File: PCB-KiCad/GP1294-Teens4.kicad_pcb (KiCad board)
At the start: 2 copper layers, 178.5 x 99.9 mm, 37 parts, among them IC1 74132D, IC2 XL6009, IC3 ZXBM5210, SW1 SW_Push, SW2 SW_Push, SW3 SW_Push, SW4 SW_Push, SW5 SW_Push, U3 R-78B5.0-2.0

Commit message: GP12.. better case and stuff
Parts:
- added R10: 100, Resistor_SMD:R_0603_1608Metric, F.Cu at (154.9, 110.2)
- added R11: 10k, Resistor_SMD:R_0603_1608Metric, F.Cu at (185.9, 74.2)
- added R12: 10k, Resistor_SMD:R_0603_1608Metric, F.Cu at (185.9, 76.7)
- added U5: ATtiny84A-P, Package_DIP:DIP-14_W7.62mm, B.Cu at (159.0, 113.3)
- added U6: 74HC165, Package_SO:SO-16_3.9x9.9mm_P1.27mm, F.Cu at (160.0, 140.0)
- added U7: 74HC165, Package_SO:SO-16_3.9x9.9mm_P1.27mm, F.Cu at (121.4, 109.5)
- SW1, SW2, SW3, SW4, SW5: value SW_Push -> SW_DPDT_x2; footprint Button_Switch_THT:SW_PUSH-12mm_Wuerth-430476085716 -> VFDs-Library:SwitchMS500Ecut
- moved SW5 82.5 mm to (111.7, 125.1)
- moved SW1 69.6 mm to (188.2, 125.0)
- moved SW4 45.2 mm to (130.8, 125.0)
- moved SW2 32.7 mm to (169.2, 125.0)
- moved R8 20.2 mm to (176.1, 69.1), turned to 180 degrees
- moved R6 20.0 mm to (167.1, 69.1), turned to 0 degrees
- moved R7 17.8 mm to (167.1, 71.6), turned to 0 degrees
- moved R9 17.5 mm to (176.0, 71.6), turned to 180 degrees
- moved R4 13.5 mm to (215.5, 74.2)
- moved IC3 11.7 mm to (215.4, 68.3)
- moved SW3 11.0 mm to (150.0, 125.0)
- moved C4 10.7 mm to (207.0, 83.6)
- moved R1 10.1 mm to (191.6, 69.3)
- moved C1 10.0 mm to (191.6, 66.3)
- moved IC1 9.40 mm to (201.7, 70.4)
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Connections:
- ENC1 pad A: unconnected-(ENC1-PadA) -> /inputs/enc1a
- ENC1 pad B: unconnected-(ENC1-PadB) -> /inputs/enc1b
- ENC1 pad C: unconnected-(ENC1-PadC) -> GND
- ENC1 pad S1: unconnected-(ENC1-PadS1) -> /inputs/enc1c
- ENC1 pad S2: unconnected-(ENC1-PadS2) -> GND
- ENC2 pad A: unconnected-(ENC2-PadA) -> /inputs/enc2a
- ENC2 pad B: unconnected-(ENC2-PadB) -> /inputs/enc2b
- ENC2 pad C: unconnected-(ENC2-PadC) -> GND
- ENC2 pad S1: unconnected-(ENC2-PadS1) -> /inputs/enc2c
- ENC2 pad S2: unconnected-(ENC2-PadS2) -> GND
- SW1 pad 1: GND -> Net-(SW1A-A)
- SW1 pad 2: Net-(U2-5) -> GND
- SW2 pad 1: unconnected-(SW2-Pad1) -> Net-(SW2A-A)
- SW2 pad 2: unconnected-(SW2-Pad2) -> GND
- SW3 pad 1: GND -> Net-(SW3A-A)
- SW3 pad 2: Net-(U2-3) -> GND
- SW4 pad 1: GND -> Net-(SW4A-A)
- SW4 pad 2: Net-(U2-4) -> GND
- SW5 pad 1: unconnected-(SW5-Pad1) -> Net-(SW5A-A)
- SW5 pad 2: unconnected-(SW5-Pad2) -> GND
- U2 pad 18: unconnected-(U2-A2-Pad18) -> /SDA
- U2 pad 19: unconnected-(U2-A3-Pad19) -> /SCL
- U2 pad 5: Net-(U2-3) -> unconnected-(U2-3-Pad5)
- U2 pad 6: Net-(U2-4) -> unconnected-(U2-4-Pad6)
- U2 pad 7: Net-(U2-5) -> unconnected-(U2-5-Pad7)
- U4 pad 11: unconnected-(U4-SDA-Pad11) -> /SDA
- U4 pad 13: unconnected-(U4-SCL-Pad13) -> /SCL
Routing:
- net GND: vias 3 -> 5
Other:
- board size 178.5 x 99.9 mm -> 178.3 x 100.1 mm

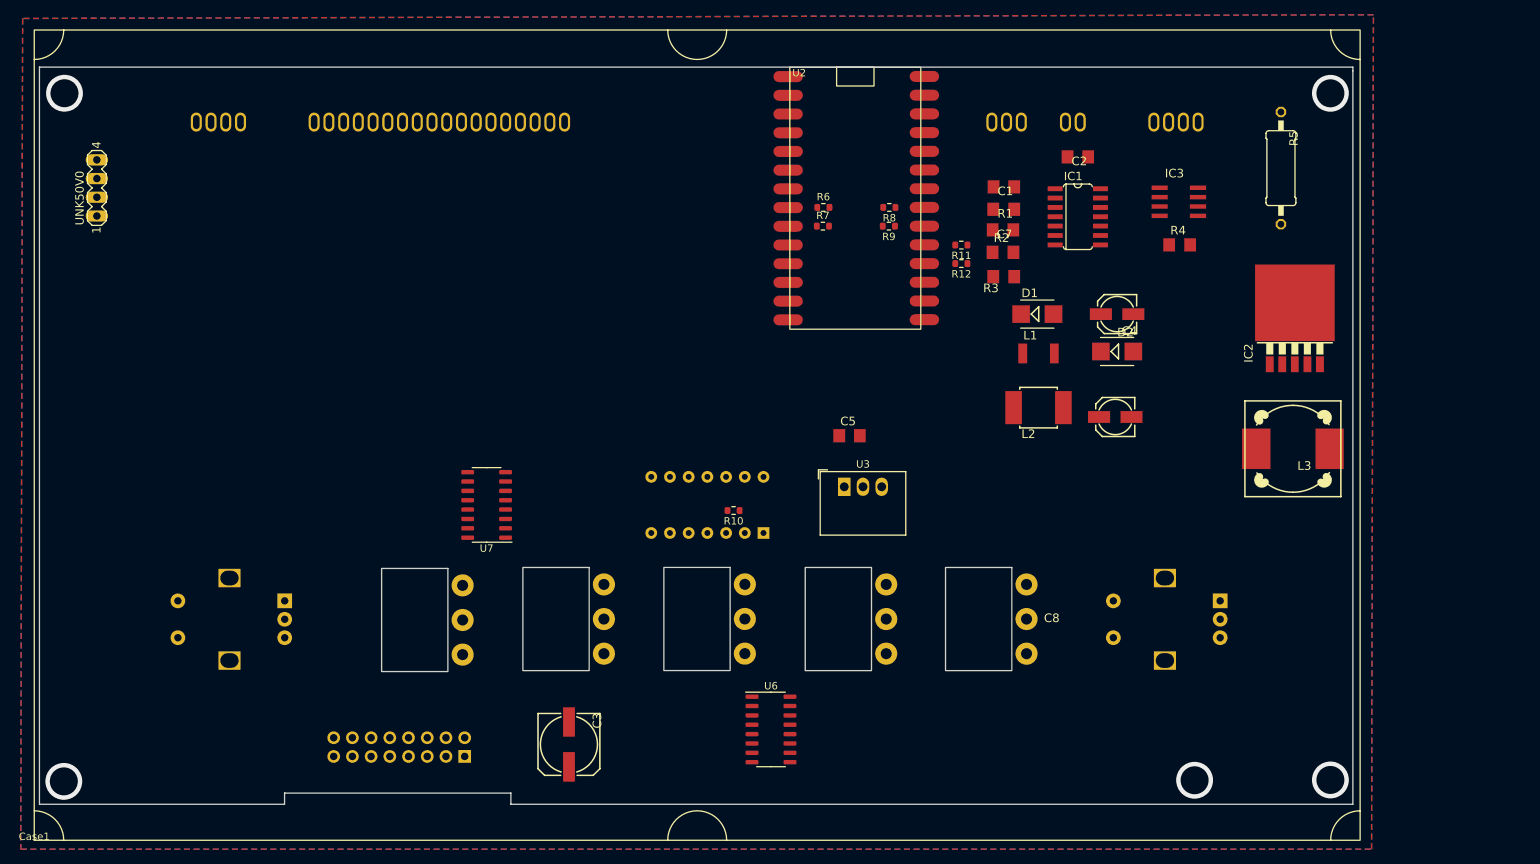
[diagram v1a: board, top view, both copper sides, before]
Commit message: GP1294 evolves
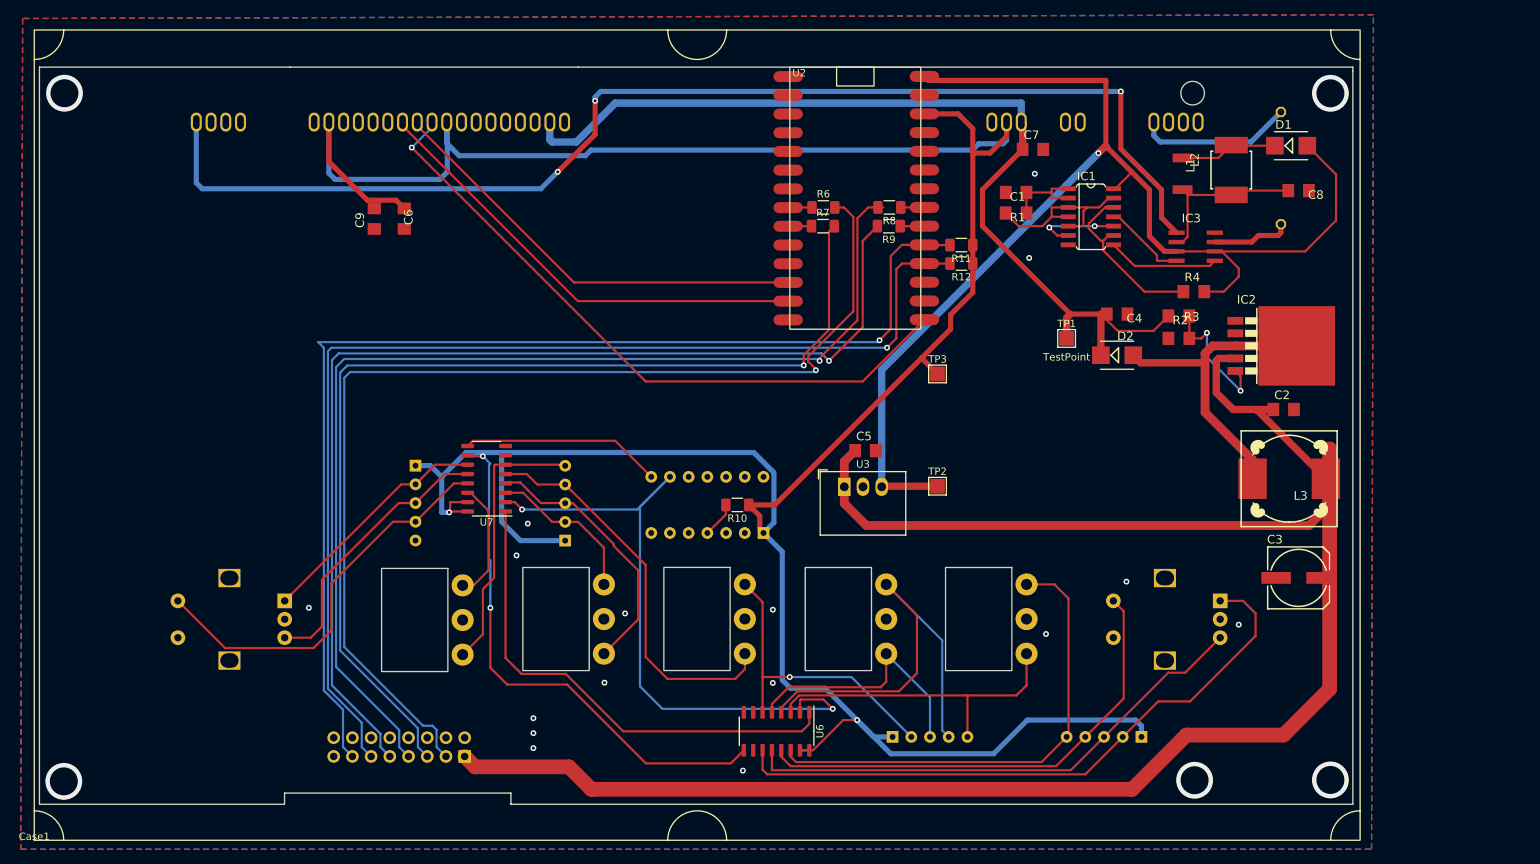
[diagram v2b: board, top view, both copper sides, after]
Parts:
- removed UNK50V0: MA04-1, VFD-Power:MA04-1
- added C6: 100n, VFD-Power:C1206, F.Cu at (110.2, 70.6)
- added C9: 1u, VFD-Power:C1206, F.Cu at (106.2, 70.6)
- added RN1: R_Network04, Resistor_THT:R_Array_SIP5, B.Cu at (210.3, 141.0)
- added RN2: R_Network04, Resistor_THT:R_Array_SIP5, B.Cu at (176.5, 141.0)
- added RN3: R_Network04, Resistor_THT:R_Array_SIP5, B.Cu at (111.8, 104.1)
- added RN4: R_Network04, Resistor_THT:R_Array_SIP5, B.Cu at (132.1, 114.3)
- added TP1: TestPoint, TestPoint:TestPoint_Pad_2.0x2.0mm, F.Cu at (200.2, 86.9)
- added TP2: +5V, TestPoint:TestPoint_Pad_2.0x2.0mm, F.Cu at (182.6, 106.9)
- added TP3: +3.3V, TestPoint:TestPoint_Pad_2.0x2.0mm, F.Cu at (182.6, 91.7)
- C4, C8: footprint VFD-Power:153CLV-0505 -> VFD-Power:C1206
- R10, R6, R7, R8, R9: footprint Resistor_SMD:R_0603_1608Metric -> Resistor_SMD:R_1206_3216Metric_Pad1.30x1.75mm_HandSolder
- R11, R12: value 10k -> 2.2k; footprint Resistor_SMD:R_0603_1608Metric -> Resistor_SMD:R_1206_3216Metric_Pad1.30x1.75mm_HandSolder
- R5: moved to B.Cu
- moved C3 101.6 mm to (231.6, 119.4), turned to 0 degrees
- moved C2 44.2 mm to (229.6, 96.5), turned to 0 degrees
- moved L2 41.5 mm to (222.5, 64.0), turned to 180 degrees
- moved D1 41.4 mm to (230.6, 60.7)
- moved C8 39.5 mm to (231.6, 66.8)
- moved L1 31.3 mm to (215.9, 64.5), turned to -90 degrees
- moved R2 25.4 mm to (215.4, 83.8), turned to 180 degrees
- moved R3 25.2 mm to (215.4, 86.9), turned to 0 degrees
- moved C7 11.7 mm to (195.6, 61.2), turned to 0 degrees
- moved R4 6.64 mm to (217.4, 80.5)
- moved IC3 6.51 mm to (217.7, 74.4)
- moved L3 4.10 mm to (230.4, 105.9)
- moved IC2 4.02 mm to (228.9, 87.9), turned to -90 degrees
- moved U7 3.56 mm to (121.4, 105.9)
- moved C5 2.96 mm to (172.8, 102.1)
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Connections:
- IC1 pad 14: +24V -> +5V
- SW1 pad 3: unconnected-(SW1A-C-Pad3) -> Net-(RN2-R4)
- SW2 pad 3: unconnected-(SW2A-C-Pad3) -> Net-(RN2-R2)
- SW3 pad 3: unconnected-(SW3A-C-Pad3) -> Net-(RN4-R3)
- SW4 pad 3: unconnected-(SW4A-C-Pad3) -> Net-(RN4-R2)
- SW5 pad 1: Net-(SW5A-A) -> Net-(RN3-R4)
- U1 pad 21: +24V -> VPP
- U1 pad 25: +24V -> VPP
- U6 pad 10: unconnected-(U6-DS-Pad10) -> GND
- U6 pad 3: unconnected-(U6-D4-Pad3) -> Net-(RN2-R4)
- U6 pad 5: unconnected-(U6-D6-Pad5) -> Net-(RN2-R2)
- U7 pad 14: unconnected-(U7-D3-Pad14) -> Net-(RN3-R4)
- U7 pad 4: unconnected-(U7-D5-Pad4) -> Net-(RN4-R2)
- U7 pad 5: Net-(SW5A-A) -> Net-(RN4-R3)
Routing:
- net +3.3V: track 0.00 -> 405.9 mm, vias 0 -> 2
- net +24V: track 0.00 -> 262.6 mm
- net +5V: track 0.00 -> 169.0 mm, vias 0 -> 1
- net F1: track 0.00 -> 165.4 mm, vias 0 -> 3
- net /SCL: track 0.00 -> 155.2 mm, vias 0 -> 1
- net /SDA: track 0.00 -> 152.3 mm, vias 0 -> 1
- net Net-(U4-MP1/MDI): track 0.00 -> 149.2 mm, vias 0 -> 1
- net Net-(U4-MP11/BCLK): track 0.00 -> 148.7 mm, vias 0 -> 1
- net Net-(U4-MP10/LRCLK): track 0.00 -> 146.3 mm, vias 0 -> 1
- net Net-(U4-MP8/MDO): track 0.00 -> 141.0 mm, vias 0 -> 1
- net VPP: track 0.00 -> 128.8 mm
- net Net-(U1-CLK): track 0.00 -> 90.8 mm, vias 0 -> 1
- net Net-(U5-PA4): track 0.00 -> 88.8 mm, vias 0 -> 2
- net /inputs/enc1a: track 0.00 -> 86.2 mm
- net Net-(U6-Q7): track 0.00 -> 71.9 mm, vias 0 -> 2
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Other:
- outline, holes or cut-outs redrawn

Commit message: Added SRC.
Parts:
- removed C4, C8: 1u, VFD-Power:C1206
- removed R6: 100, Resistor_SMD:R_1206_3216Metric_Pad1.30x1.75mm_HandSolder
- added U8: CS8421, VFDs-Library:CS8421-breakout-smd, F.Cu at (137.5, 79.2)
- moved R8 61.1 mm to (116.3, 82.0)
- moved R9 60.1 mm to (116.4, 78.5)
- moved R7 52.6 mm to (116.3, 85.6), turned to 180 degrees
- turned C9 to -90 degrees
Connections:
- R7 pad 1: /IN1 -> /DATA_OUT
- R8 pad 1: /BCLK1 -> /BCK_OUT
- R9 pad 1: /LRCLK1 -> /LRCK_OUT
- U4 pad 3: Net-(U4-MP1/MDI) -> unconnected-(U4-MP1/MDI-Pad3)
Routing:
- net Net-(U4-MP1/MDI): track 149.2 -> 0.00 mm, vias 1 -> 0
- net Net-(U4-MP11/BCLK): track 148.7 -> 74.8 mm
- net Net-(U4-MP10/LRCLK): track 146.3 -> 77.3 mm
- net Net-(U4-MP8/MDO): track 141.0 -> 73.3 mm
- net /LRCLK1: track 3.28 -> 54.5 mm
- net /BCLK1: track 3.21 -> 54.2 mm
- net /OUT1: track 3.24 -> 41.3 mm
- net +3.3V: track 405.9 -> 441.4 mm, vias 2 -> 3
- net Net-(RN3-R4): track 16.3 -> 26.5 mm
- net /DATA_OUT: track 0.00 -> 6.76 mm
- net /BCK_OUT: track 0.00 -> 6.34 mm
- net /LRCK_OUT: track 0.00 -> 5.90 mm
- net Net-(U1-DIO): track 62.7 -> 66.9 mm
- net Net-(U1-CS): track 59.7 -> 63.4 mm
- net /IN1: track 3.18 -> 0.00 mm
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
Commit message: grummel
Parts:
- added C4: 1u, VFD-Power:C1206, F.Cu at (260.2, 91.7)
- added C8: 1u, VFD-Power:C1206, F.Cu at (260.2, 94.7)
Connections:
- U1 pad 9: unconnected-(U1-TEST-Pad9) -> +3.3V
- U8 pad 5: /DATA_OUT -> unconnected-(U8-DATA_OUT-Pad5)
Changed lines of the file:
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@@
   (net 4 "unconnected-(U1-NC-Pad7)")
   (net 5 "unconnected-(U1-NC-Pad8)")
-  (net 6 "unconnected-(U1-TEST-Pad9)")
+  (net 6 "unconnected-(U8-DATA_OUT-Pad5)")
   (net 7 "unconnected-(U1-RESET-Pad10)")
   (net 8 "unconnected-(U1-INT-Pad15)")
@@
       (net 97 "/BCK_OUT") (pinfunction "BCK_OUT") (pintype "output"))
     (pad "5" smd oval (at -13.97 3.81) (size 4 1.524) (layers "F.Cu" "F.Paste" "F.Mask")
-      (net 98 "/DATA_OUT") (pinfunction "DATA_OUT") (pintype "output"))
+      (net 6 "unconnected-(U8-DATA_OUT-Pad5)") (pinfunction "DATA_OUT") (pintype "output"))
     (pad "6" smd oval (at -13.97 6.35) (size 4 1.524) (layers "F.Cu" "F.Paste" "F.Mask")
       (net 99 "unconnected-(U8-MCLK_OUT-Pad6)") (pinfunction "MCLK_OUT") (pintype "output"))
@@
     )
   )
+  (footprint "VFD-Power:C1206" (layer "F.Cu")
+    (at 260.22 94.742)
+    (descr "<b>CAPACITOR</b>")
+    (property "Sheetfile" "VFD-Power.kicad_sch")
+    (property "Sheetname" "Power")
+    (fp_text reference "C8" (at -1.27 -1.27) (layer "F.SilkS")
+        (effects (font (size 1.1684 1.1684) (thickness 0.1016)) (justify left bottom))
+    )
+    (fp_text value "1u" (at -1.27 2.54) (layer "F.Fab")
+        (effects (font (size 1.1684 1.1684) (thickness 0.1016)) (justify left bottom))
+    )
+    (fp_poly
+      (pts
+        (xy -0.1999 0.4001)
+        (xy 0.1999 0.4001)
+        (xy 0.1999 -0.4001)
+        (xy -0.1999 -0.4001)
+      )
+      (stroke (width 0) (type default)) (fill solid) (layer "F.Adhes"))
+    (fp_line (start -2.473 -0.983) (end 2.473 -0.983)
+      (stroke (width 0.0508) (type solid)) (layer "F.CrtYd"))
+    (fp_line (start -2.473 0.983) (end -2.473 -0.983)
+      (stroke (width 0.0508) (type solid)) (layer "F.CrtYd"))
+    (fp_line (start 2.473 -0.983) (end 2.473 0.983)
+      (stroke (width 0.0508) (type solid)) (layer "F.CrtYd"))
+    (fp_line (start 2.473 0.983) (end -2.473 0.983)
+      (stroke (width 0.0508) (type solid)) (layer "F.CrtYd"))
+    (fp_line (start -0.965 -0.787) (end 0.965 -0.787)
+      (stroke (width 0.1016) (type solid)) (layer "F.Fab"))
+    (fp_line (start -0.965 0.787) (end 0.965 0.787)
+      (stroke (width 0.1016) (type solid)) (layer "F.Fab"))
+    (fp_poly
+      (pts
+        (xy -1.7018 0.8509)
+        (xy -0.9517 0.8509)
+        (xy -0.9517 -0.8491)
+        (xy -1.7018 -0.8491)
+      )
+      (stroke (width 0) (type default)) (fill solid) (layer "F.Fab"))
+    (fp_poly
+      (pts
+        (xy 0.9517 0.8491)
+        (xy 1.7018 0.8491)
+        (xy 1.7018 -0.8509)
+        (xy 0.9517 -0.8509)
+      )
+      (stroke (width 0) (type default)) (fill solid) (layer "F.Fab"))
+    (pad "1" smd rect (at -1.4 0) (size 1.6 1.8) (layers "F.Cu" "F.Paste" "F.Mask")
+      (solder_mask_margin 0.0508) (thermal_bridge_angle 0))
+    (pad "2" smd rect (at 1.4 0) (size 1.6 1.8) (layers "F.Cu" "F.Paste" "F.Mask")
+      (solder_mask_margin 0.0508) (thermal_bridge_angle 0))
+  )
   (footprint "VFD-Power:SO14" (layer "F.Cu")
     (at 203.454 70.358 -90)
@@
     )
   )
+  (footprint "VFD-Power:C1206" (layer "F.Cu")
+    (at 260.22 91.7252)
+    (descr "<b>CAPACITOR</b>")
+    (property "Sheetfile" "VFD-Power.kicad_sch")
+    (property "Sheetname" "Power")
+    (fp_text reference "C4" (at -1.27 -1.27) (layer "F.SilkS")
+        (effects (font (size 1.1684 1.1684) (thickness 0.1016)) (justify left bottom))
+    )
+    (fp_text value "1u" (at -1.27 2.54) (layer "F.Fab")
+        (effects (font (size 1.1684 1.1684) (thickness 0.1016)) (justify left bottom))
+    )
+    (fp_poly
+      (pts
+        (xy -0.1999 0.4001)
+        (xy 0.1999 0.4001)
+        (xy 0.1999 -0.4001)
+        (xy -0.1999 -0.4001)
+      )
+      (stroke (width 0) (type default)) (fill solid) (layer "F.Adhes"))
+    (fp_line (start -2.473 -0.983) (end 2.473 -0.983)
+      (stroke (width 0.0508) (type solid)) (layer "F.CrtYd"))
+    (fp_line (start -2.473 0.983) (end -2.473 -0.983)
+      (stroke (width 0.0508) (type solid)) (layer "F.CrtYd"))
+    (fp_line (start 2.473 -0.983) (end 2.473 0.983)
+      (stroke (width 0.0508) (type solid)) (layer "F.CrtYd"))
+    (fp_line (start 2.473 0.983) (end -2.473 0.983)
+      (stroke (width 0.0508) (type solid)) (layer "F.CrtYd"))
+    (fp_line (start -0.965 -0.787) (end 0.965 -0.787)
+      (stroke (width 0.1016) (type solid)) (layer "F.Fab"))
+    (fp_line (start -0.965 0.787) (end 0.965 0.787)
+      (stroke (width 0.1016) (type solid)) (layer "F.Fab"))
+    (fp_poly
+      (pts
+        (xy -1.7018 0.8509)
+        (xy -0.9517 0.8509)
+        (xy -0.9517 -0.8491)
+        (xy -1.7018 -0.8491)
+      )
+      (stroke (width 0) (type default)) (fill solid) (layer "F.Fab"))
+    (fp_poly
+      (pts
+        (xy 0.9517 0.8491)
+        (xy 1.7018 0.8491)
+        (xy 1.7018 -0.8509)
+        (xy 0.9517 -0.8509)
+      )
+      (stroke (width 0) (type default)) (fill solid) (layer "F.Fab"))
+    (pad "1" smd rect (at -1.4 0) (size 1.6 1.8) (layers "F.Cu" "F.Paste" "F.Mask")
+      (solder_mask_margin 0.0508) (thermal_bridge_angle 0))
+    (pad "2" smd rect (at 1.4 0) (size 1.6 1.8) (layers "F.Cu" "F.Paste" "F.Mask")
+      (solder_mask_margin 0.0508) (thermal_bridge_angle 0))
+  )
   (footprint "TestPoint:TestPoint_Pad_2.0x2.0mm" (layer "F.Cu")
     (at 200.152 86.868)
@@
       (net 5 "unconnected-(U1-NC-Pad8)") (pinfunction "NC") (pintype "no_connect"))
     (pad "9" thru_hole oval locked (at 44 22.5 180) (size 1.5 2.6) (drill oval 0.9 1.9) (layers "*.Cu" "*.Mask")
-      (net 6 "unconnected-(U1-TEST-Pad9)") (pinfunction "TEST") (pintype "input"))
+      (net 18 "+3.3V") (pinfunction "TEST") (pintype "input"))
     (pad "10" thru_hole oval locked (at 42 22.5 180) (size 1.5 2.6) (drill oval 0.9 1.9) (layers "*.Cu" "*.Mask")
       (net 7 "unconnected-(U1-RESET-Pad10)") (pinfunction "RESET") (pintype "input"))

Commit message: Fixed merge issues.
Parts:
- removed C8: 1u, VFD-Power:C1206
- added C10: 1u, Capacitor_SMD:C_1206_3216Metric_Pad1.33x1.80mm_HandSolder, F.Cu at (204.0, 83.8)
- C4: footprint VFD-Power:C1206 -> Capacitor_SMD:C_1206_3216Metric_Pad1.33x1.80mm_HandSolder
- moved C4 38.6 mm to (230.7, 66.8)
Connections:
- C4 pad 1: (no net) -> Net-(IC3-VM)
- C4 pad 2: (no net) -> GND
- U8 pad 5: unconnected-(U8-DATA_OUT-Pad5) -> /DATA_OUT
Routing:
- net +3.3V: track 441.4 -> 449.2 mm
- net +24V: track 262.6 -> 258.7 mm
